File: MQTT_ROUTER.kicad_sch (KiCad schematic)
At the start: 20 parts, among them J1 Conn_2Rows-07Pins, J2 Conn_02x07_Odd_Even, Q3 BSS138, SW1 SW_Push, U1 ESP32-DevKitC, U2 TXS0108EPW

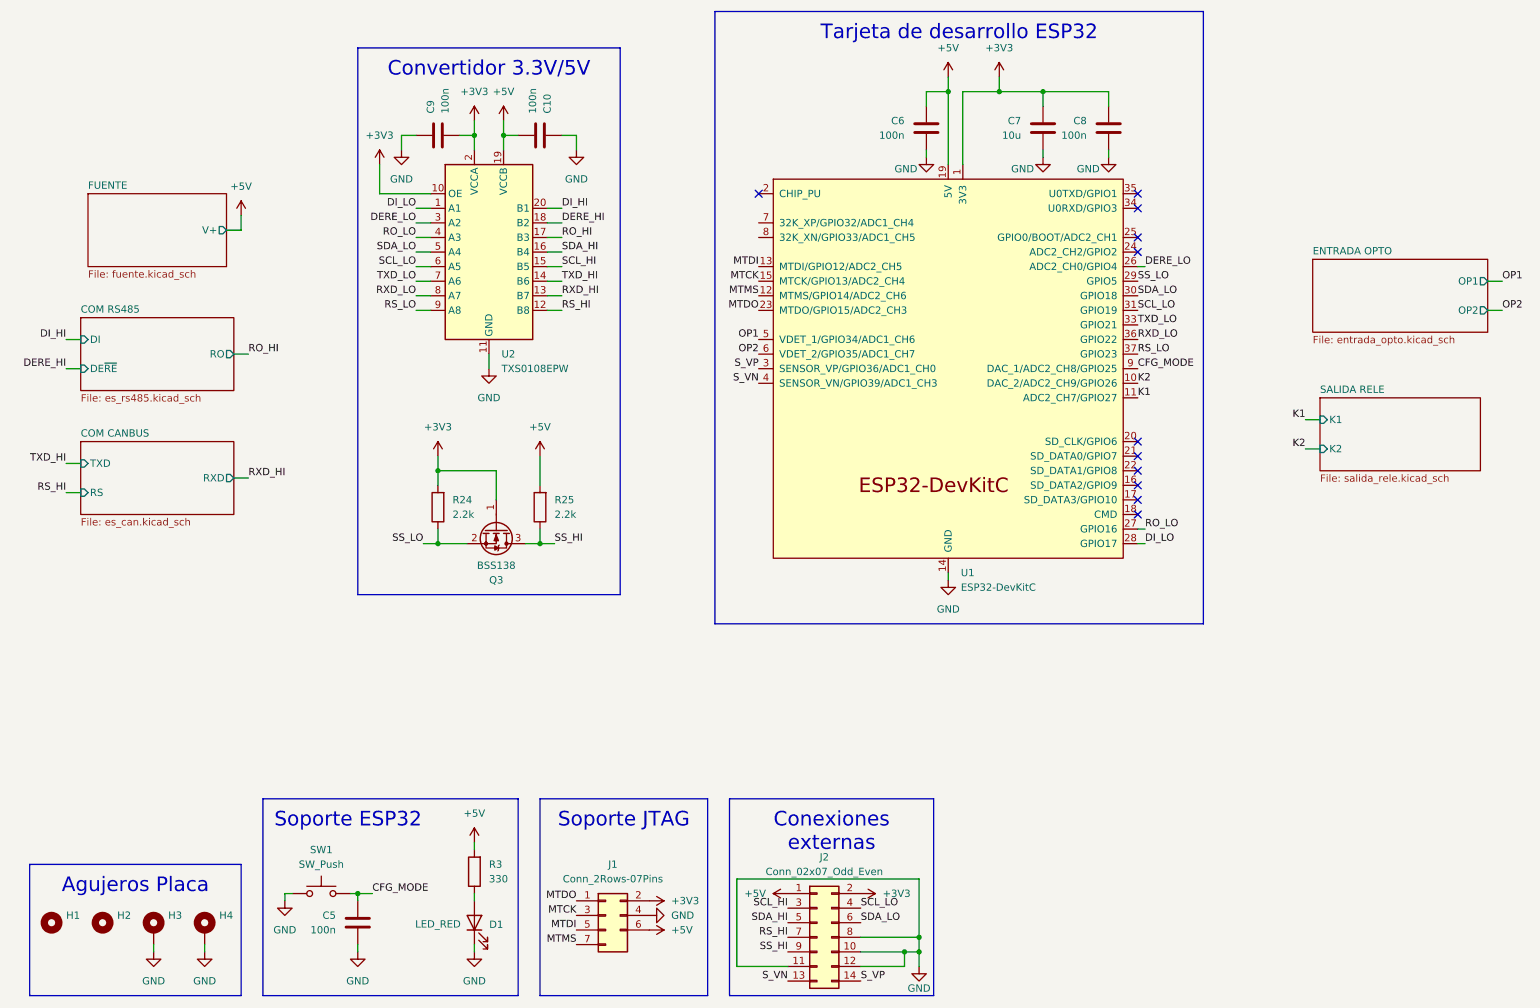
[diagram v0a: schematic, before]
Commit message: Actualizar componentes, pistas e imágenes
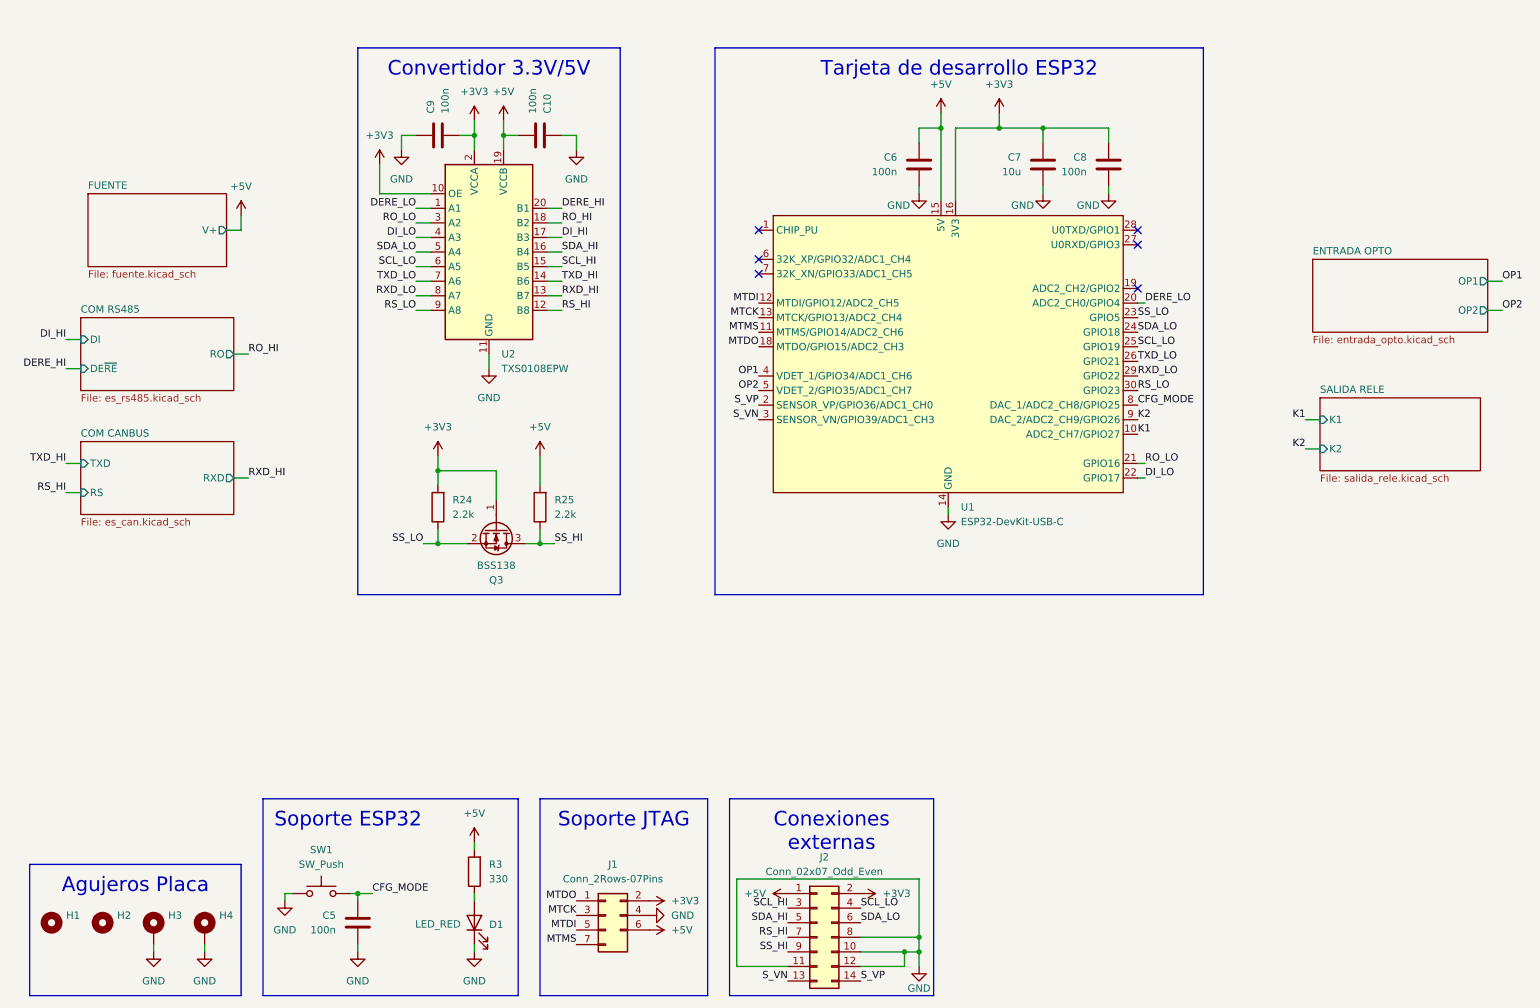
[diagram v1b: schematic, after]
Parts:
- removed U1: ESP32-DevKitC, PCM_Espressif:ESP32-DevKitC, symbol PCM_Espressif:ESP32-DevKitC
- added U1: ESP32-DevKit-USB-C, ESP32:ESP32-DevKit-USB-C, symbol ESP32:ESP32-DevKit-USB-C
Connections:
- net +3V3: now also U1.16 (3V3)
- net +5V: now also U1.15 (5V)
- net CFG_MODE: now also U1.8 (DAC_1/ADC2_CH8/GPIO25)
- net DERE_HI: now also U2.20 (B1); no longer U2.18 (B2)
- net DERE_LO: now also U2.1 (A1), U1.20 (ADC2_CH0/GPIO4); no longer U2.3 (A2)
- net DI_HI: now also U2.17 (B3); no longer U2.20 (B1)
- net DI_LO: now also U2.4 (A3), U1.22 (GPIO17); no longer U2.1 (A1)
- net GND: now also U1.14 (GND), U1.17 (GND)
- net K1: now also U1.10 (ADC2_CH7/GPIO27)
- net K2: now also U1.9 (DAC_2/ADC2_CH9/GPIO26)
- net MTCK: now also U1.13 (MTCK/GPIO13/ADC2_CH4)
- net MTDI: now also U1.12 (MTDI/GPIO12/ADC2_CH5)
- net MTDO: now also U1.18 (MTDO/GPIO15/ADC2_CH3)
- net MTMS: now also U1.11 (MTMS/GPIO14/ADC2_CH6)
- net OP1: now also U1.4 (VDET_1/GPIO34/ADC1_CH6)
- net OP2: now also U1.5 (VDET_2/GPIO35/ADC1_CH7)
- net RO_HI: now also U2.18 (B2); no longer U2.17 (B3)
- net RO_LO: now also U2.3 (A2), U1.21 (GPIO16); no longer U2.4 (A3)
- net RS_LO: now also U1.30 (GPIO23)
- net RXD_LO: now also U1.29 (GPIO22)
- net SCL_LO: now also U1.25 (GPIO19)
- net SDA_LO: now also U1.24 (GPIO18)
- net SS_LO: now also U1.23 (GPIO5)
- net S_VN: now also U1.3 (SENSOR_VN/GPIO39/ADC1_CH3)
- net S_VP: now also U1.2 (SENSOR_VP/GPIO36/ADC1_CH0)
- net TXD_LO: now also U1.26 (GPIO21)
- no-connect marks 11 -> 6
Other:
- moved on the sheet: C6, C7, C8

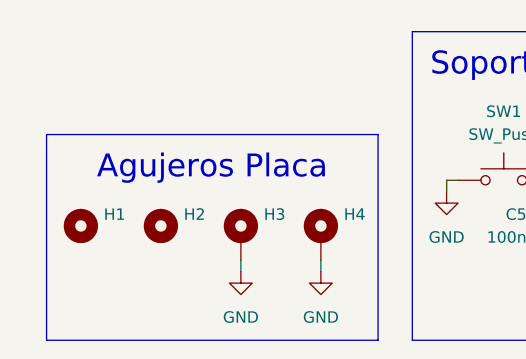
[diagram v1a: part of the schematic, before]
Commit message: Cambiar agujeros de placa, invertir terminales de fuente
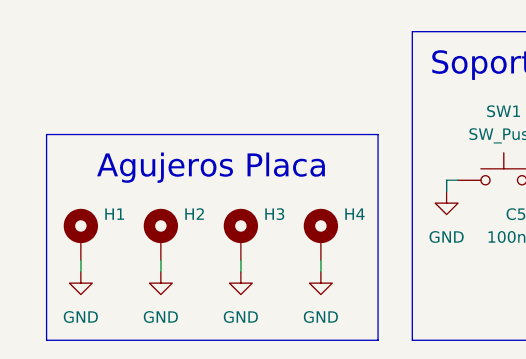
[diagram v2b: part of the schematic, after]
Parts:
- removed H1, H2: MountingHole, MountingHole:MountingHole_3.5mm, symbol Mechanical:MountingHole
- added H1, H2: MountingHole_Pad, MountingHole:MountingHole_3.5mm_Pad_Via, symbol Mechanical:MountingHole_Pad
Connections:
- net GND: now also H1.1, H2.1
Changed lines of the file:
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@@
 	(wire
 		(pts
+			(xy 27.94 185.42) (xy 27.94 186.69)
+		)
+		(stroke
+			(width 0)
+			(type default)
+		)
+	)
+	(wire
+		(pts
 			(xy 105.41 72.39) (xy 107.95 72.39)
 		)
@@
 	(wire
 		(pts
+			(xy 19.05 185.42) (xy 19.05 186.69)
+		)
+		(stroke
+			(width 0)
+			(type default)
+		)
+	)
+	(wire
+		(pts
 			(xy 104.14 113.03) (xy 104.14 115.57)
 		)
@@
 	)
 	(symbol
+		(lib_id "Mechanical:MountingHole_Pad")
+		(at 27.94 182.88 0)
+		(unit 1)
+		(exclude_from_sim yes)
+		(in_bom no)
+		(on_board yes)
+		(dnp no)
+		(fields_autoplaced yes)
+		(property "Reference" "H2"
+			(at 30.48 180.3399 0)
+			(effects
+				(font
+					(size 1.27 1.27)
+				)
+				(justify left)
+			)
+		)
+		(property "Value" "MountingHole_Pad"
+			(at 30.48 182.8799 0)
+			(effects
+				(font
+					(size 1.27 1.27)
+				)
+				(justify left)
+				(hide yes)
+			)
+		)
+		(property "Footprint" "MountingHole:MountingHole_3.5mm_Pad_Via"
+			(at 27.94 182.88 0)
+			(effects
+				(font
+					(size 1.27 1.27)
+				)
+				(hide yes)
+			)
+		)
+		(property "Datasheet" "~"
+			(at 27.94 182.88 0)
+			(effects
+				(font
+					(size 1.27 1.27)
+				)
+				(hide yes)
+			)
+		)
+		(property "Description" "Mounting Hole with connection"
+			(at 27.94 182.88 0)
+			(effects
+				(font
+					(size 1.27 1.27)
+				)
+				(hide yes)
+			)
+		)
+		(pin "1"
+		)
+		(instances
+			(project "MQTT_ROUTER"
+				(path "/0145d1be-ca61-471a-b9b5-114658e6a523"
+					(reference "H2")
+					(unit 1)
+				)
+			)
+		)
+	)
+	(symbol
 		(lib_id "Device:R")
 		(at 92.71 172.72 180)
@@
 	)
 	(symbol
+		(lib_id "power:GND")
+		(at 19.05 186.69 0)
+		(unit 1)
+		(exclude_from_sim no)
+		(in_bom yes)
+		(on_board yes)
+		(dnp no)
+		(fields_autoplaced yes)
+		(property "Reference" "#PWR61"
+			(at 19.05 193.04 0)
+			(effects
+				(font
+					(size 1.27 1.27)
+				)
+				(hide yes)
+			)
+		)
+		(property "Value" "GND"
+			(at 19.05 191.77 0)
+			(effects
+				(font
+					(size 1.27 1.27)
+				)
+			)
+		)
+		(property "Footprint" ""
+			(at 19.05 186.69 0)
+			(effects
+				(font
+					(size 1.27 1.27)
+				)
+				(hide yes)
+			)
+		)
+		(property "Datasheet" ""
+			(at 19.05 186.69 0)
+			(effects
+				(font
+					(size 1.27 1.27)
+				)
+				(hide yes)
+			)
+		)
+		(property "Description" "Power symbol creates a global label with name \"GND\" , ground"
+			(at 19.05 186.69 0)
+			(effects
+				(font
+					(size 1.27 1.27)
+				)
+				(hide yes)
+			)
+		)
+		(pin "1"
+		)
+		(instances
+			(project "MQTT_ROUTER"
+				(path "/0145d1be-ca61-471a-b9b5-114658e6a523"
+					(reference "#PWR61")
+					(unit 1)
+				)
+			)
+		)
+	)
+	(symbol
 		(lib_id "Device:C")
 		(at 203.2 49.53 0)
@@
 	(symbol
 		(lib_id "Mechanical:MountingHole_Pad")
+		(at 19.05 182.88 0)
+		(unit 1)
+		(exclude_from_sim yes)
+		(in_bom no)
+		(on_board yes)
+		(dnp no)
+		(fields_autoplaced yes)
+		(property "Reference" "H1"
+			(at 21.59 180.3399 0)
+			(effects
+				(font
+					(size 1.27 1.27)
+				)
+				(justify left)
+			)
+		)
+		(property "Value" "MountingHole_Pad"
+			(at 21.59 182.8799 0)
+			(effects
+				(font
+					(size 1.27 1.27)
+				)
+				(justify left)
+				(hide yes)
+			)
+		)
+		(property "Footprint" "MountingHole:MountingHole_3.5mm_Pad_Via"
+			(at 19.05 182.88 0)
+			(effects
+				(font
+					(size 1.27 1.27)
+				)
+				(hide yes)
+			)
+		)
+		(property "Datasheet" "~"
+			(at 19.05 182.88 0)
+			(effects
+				(font
+					(size 1.27 1.27)
+				)
+				(hide yes)
+			)
+		)
+		(property "Description" "Mounting Hole with connection"
+			(at 19.05 182.88 0)
+			(effects
+				(font
+					(size 1.27 1.27)
+				)
+				(hide yes)
+			)
+		)
+		(pin "1"
+		)
+		(instances
+			(project "MQTT_ROUTER"
+				(path "/0145d1be-ca61-471a-b9b5-114658e6a523"
+					(reference "H1")
+					(unit 1)
+				)
+			)
+		)
+	)
+	(symbol
+		(lib_id "Mechanical:MountingHole_Pad")
 		(at 45.72 182.88 0)
 		(unit 1)
@@
 	(symbol
 		(lib_id "power:GND")
+		(at 27.94 186.69 0)
+		(unit 1)
+		(exclude_from_sim no)
+		(in_bom yes)
+		(on_board yes)
+		(dnp no)
+		(fields_autoplaced yes)
+		(property "Reference" "#PWR62"
+			(at 27.94 193.04 0)
+			(effects
+				(font
+					(size 1.27 1.27)
+				)
+				(hide yes)
+			)
+		)
+		(property "Value" "GND"
+			(at 27.94 191.77 0)
+			(effects
+				(font
+					(size 1.27 1.27)
+				)
+			)
+		)
+		(property "Footprint" ""
+			(at 27.94 186.69 0)
+			(effects
+				(font
+					(size 1.27 1.27)
+				)
+				(hide yes)
+			)
+		)
+		(property "Datasheet" ""
+			(at 27.94 186.69 0)
+			(effects
+				(font
+					(size 1.27 1.27)
+				)
+				(hide yes)
+			)
+		)
+		(property "Description" "Power symbol creates a global label with name \"GND\" , ground"
+			(at 27.94 186.69 0)
+			(effects
+				(font
+					(size 1.27 1.27)
+				)
+				(hide yes)
+			)
+		)
+		(pin "1"
+		)
+		(instances
+			(project "MQTT_ROUTER"
+				(path "/0145d1be-ca61-471a-b9b5-114658e6a523"
+					(reference "#PWR62")
+					(unit 1)
+				)
+			)
+		)
+	)
+	(symbol
+		(lib_id "power:GND")
 		(at 36.83 186.69 0)
 		(unit 1)
@@
 	)
 	(symbol
-		(lib_id "Mechanical:MountingHole")
-		(at 27.94 181.61 0)
-		(unit 1)
-		(exclude_from_sim yes)
-		(in_bom no)
-		(on_board yes)
-		(dnp no)
-		(fields_autoplaced yes)
-		(property "Reference" "H2"
-			(at 30.48 180.3399 0)
-			(effects
-				(font
-					(size 1.27 1.27)
-				)
-				(justify left)
-			)
-		)
-		(property "Value" "MountingHole"
-			(at 30.48 182.8799 0)
-			(effects
-				(font
-					(size 1.27 1.27)
-				)
-				(justify left)
-				(hide yes)
-			)
-		)
-		(property "Footprint" "MountingHole:MountingHole_3.5mm"
-			(at 27.94 181.61 0)
-			(effects
-				(font
-					(size 1.27 1.27)
-				)
-				(hide yes)
-			)
-		)
-		(property "Datasheet" "~"
-			(at 27.94 181.61 0)
-			(effects
-				(font
-					(size 1.27 1.27)
-				)
-				(hide yes)
-			)
-		)
-		(property "Description" "Mounting Hole without connection"
-			(at 27.94 181.61 0)
-			(effects
-				(font
-					(size 1.27 1.27)
-				)
-				(hide yes)
-			)
-		)
-		(instances
-			(project "MQTT_ROUTER"
-				(path "/0145d1be-ca61-471a-b9b5-114658e6a523"
-					(reference "H2")
-					(unit 1)
-				)
-			)
-		)
-	)
-	(symbol
 		(lib_id "power:GND")
 		(at 170.18 189.23 0)
@@
 					(unit 1)
 				)
-			)
-		)
-	)
-	(symbol
-		(lib_id "Mechanical:MountingHole")
-		(at 19.05 181.61 0)
-		(unit 1)
-		(exclude_from_sim yes)
-		(in_bom no)
-		(on_board yes)
-		(dnp no)
-		(fields_autoplaced yes)
-		(property "Reference" "H1"
-			(at 21.59 180.3399 0)
-			(effects
-				(font
-					(size 1.27 1.27)
-				)
-				(justify left)
-			)
-		)
-		(property "Value" "MountingHole"
-			(at 21.59 182.8799 0)
-			(effects
-				(font
-					(size 1.27 1.27)
-				)
-				(justify left)
-				(hide yes)
-			)
-		)
-		(property "Footprint" "MountingHole:MountingHole_3.5mm"
-			(at 19.05 181.61 0)
-			(effects
-				(font
-					(size 1.27 1.27)
-				)
-				(hide yes)
-			)
-		)
-		(property "Datasheet" "~"
-			(at 19.05 181.61 0)
-			(effects
-				(font
-					(size 1.27 1.27)
-				)
-				(hide yes)
-			)
-		)
-		(property "Description" "Mounting Hole without connection"
-			(at 19.05 181.61 0)
-			(effects
-				(font
-					(size 1.27 1.27)
-				)
-				(hide yes)
-			)
-		)
-		(instances
-			(project ""
-				(path "/0145d1be-ca61-471a-b9b5-114658e6a523"
-					(reference "H1")
-					(unit 1)
-				)
